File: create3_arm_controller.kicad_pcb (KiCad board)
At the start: 2 copper layers, 229.5 x 111 mm, 178 parts, among them IC1 TPS40192DRCT-TPS40192DRCT, J1 USB_C_Receptacle, J10 Conn_01x22_Female, J11 690-019-298-412, J12 Barrel_Jack, J13 Conn_01x02_Female, J14 Molex 470531000, J15 USB_OTG, J16 690-008-221-904, J17 Conn_01x03_Female, J18 Conn_01x03_Female, J19 Conn_01x03_Female, J2 USB_C_Receptacle, J20 Conn_01x03_Female, J21 Conn_01x03_Female, J22 Conn_01x03_Female, J23 Conn_01x03_Female, J24 Conn_01x03_Female, J25 Conn_01x03_Female, J26 Conn_01x03_Female, J27 Conn_01x03_Female, J28 Conn_01x03_Female, J4 Conn_02x07_Odd_Even, J5 Conn_01x03, J6 Conn_01x03, J7 THD-20-R, J8 Micro_SD_Card_Det, J9 Conn_01x22_Female, Q1 BUK9M17-30EX / BUK7M10-40E, Q2 BUK9M17-30EX / BUK7M10-40E, Q3 DMP3013SFV-7, U1 TUSB7340, U10 EMC2301-1-ACZL-TR, U11 74LVC1G07SE-7, U12 FSUSB42MUX, U13 USB2514B-I/M2, U14 TPD4EUSB30, U15 AP22653W6, U16 STM32F303VETx, U2 TPS2560, U3 TPS2560, U4 74LVC1G07SE-7, U5 74LVC1G07SE-7, U6 RT9742GGJ5, U7 RT9742SNGV, U8 AP64501SP-13, U9 PCF85063AT/AAZ, Y1 Crystal_Small, Y2 X32K768S301, Y3 24MHz

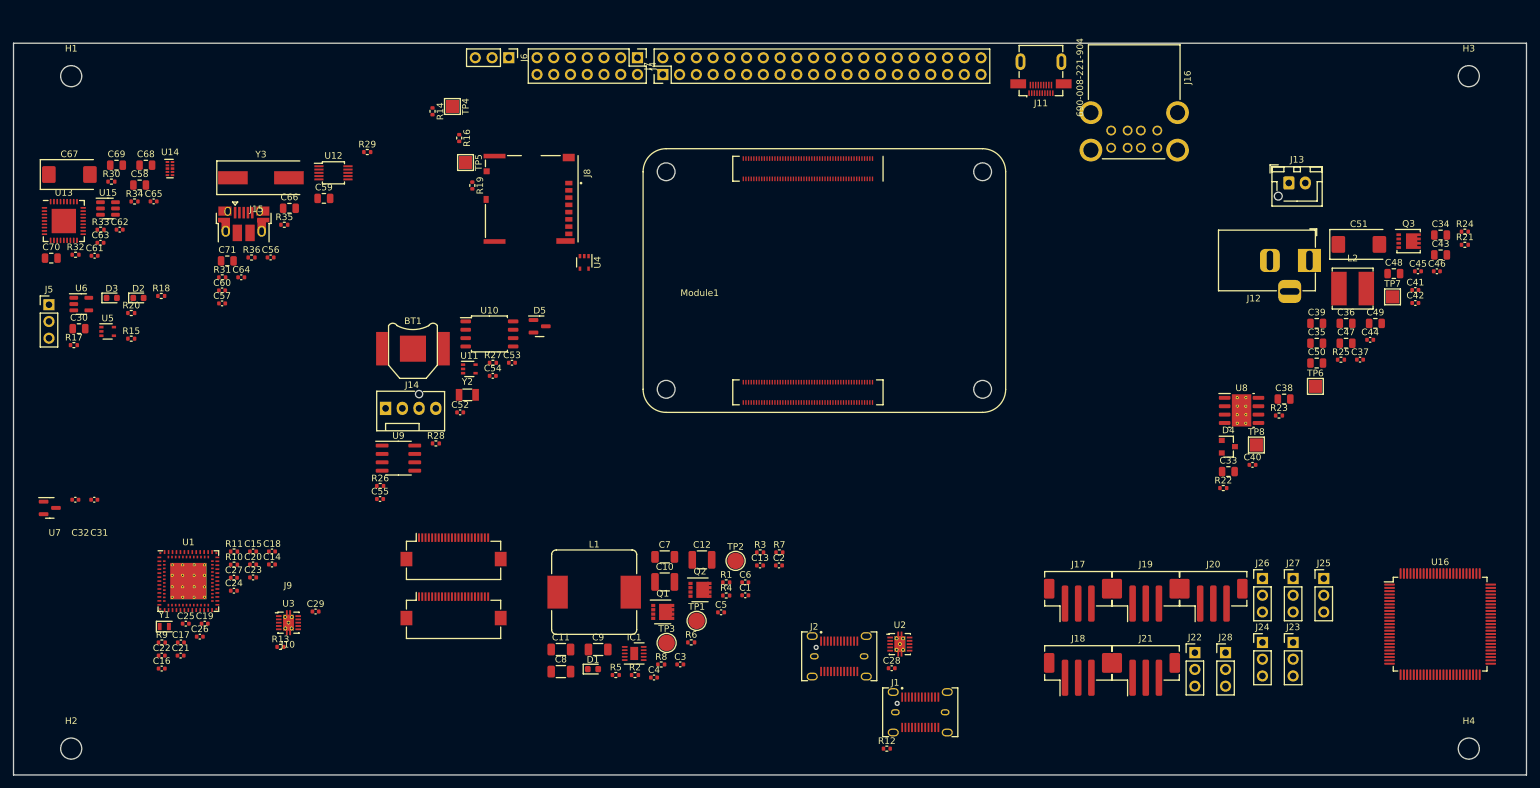
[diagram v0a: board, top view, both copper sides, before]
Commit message: Initial layout and all parts added. Some pins still not connected to power
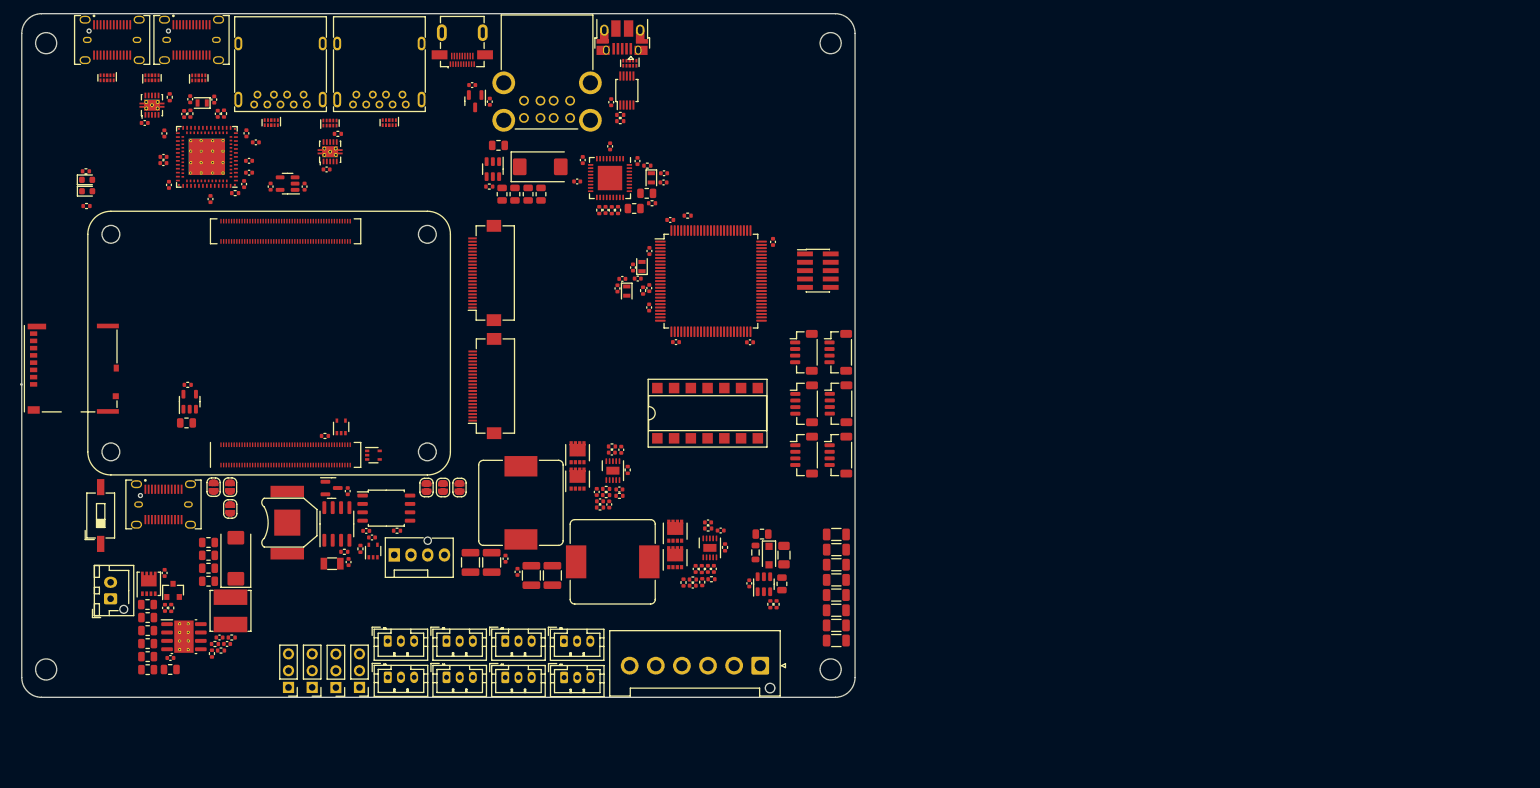
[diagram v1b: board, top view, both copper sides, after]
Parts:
- removed D1: LED, LED_SMD:LED_0603_1608Metric
- removed D2: LED Green, LED_SMD:LED_0603_1608Metric
- removed R16: nf, Resistor_SMD:R_0402_1005Metric
- removed R6: 100k, Resistor_SMD:R_0402_1005Metric
- removed R9: 4.7K, Resistor_SMD:R_0402_1005Metric
- removed TP1: Batt+, TestPoint:TestPoint_Pad_D2.5mm
- removed TP2: GND, TestPoint:TestPoint_Pad_D2.5mm
- removed TP3: 6V, TestPoint:TestPoint_Pad_D2.5mm
- removed TP4, TP5, TP6, TP7, TP8: TestPoint, TestPoint:TestPoint_Pad_2.0x2.0mm
- added C72: 10uF 35v, Capacitor_SMD:C_0805_2012Metric, F.Cu at (52.1, 126.0)
- added C73: 1.2nF, Capacitor_SMD:C_0402_1005Metric, F.Cu at (64.1, 122.1)
- added C74: 10uF, Capacitor_SMD:C_0805_2012Metric, F.Cu at (61.3, 106.7)
- added C75: 10uF, Capacitor_SMD:C_0805_2012Metric, F.Cu at (61.3, 110.6)
- added C76: 10uF, Capacitor_SMD:C_0805_2012Metric, F.Cu at (61.3, 112.6)
- added C77: 10uF, Capacitor_SMD:C_0805_2012Metric, F.Cu at (61.3, 108.7)
- added C78: 100uF, Capacitor_Tantalum_SMD:CP_EIA-7343-31_Kemet-D, F.Cu at (65.5, 109.1)
- added C79: 100nF, Capacitor_SMD:C_0402_1005Metric, F.Cu at (82.5, 99.0)
- added C80: 100nF, Capacitor_SMD:C_0402_1005Metric, F.Cu at (85.3, 105.0)
- added C81: 100nF, Capacitor_SMD:C_0402_1005Metric, F.Cu at (86.1, 106.0)
- added C82: 100nF, Capacitor_SMD:C_0402_1005Metric, F.Cu at (82.6, 109.7)
- added C83: 27pF, Capacitor_SMD:C_0402_1005Metric, F.Cu at (130.4, 50.7)
- added C84: 27pF, Capacitor_SMD:C_0402_1005Metric, F.Cu at (130.4, 52.1)
- added C85: 10uF, Capacitor_SMD:C_0805_2012Metric, F.Cu at (127.8, 53.8)
- added C86: 10uF, Capacitor_SMD:C_0805_2012Metric, F.Cu at (125.9, 56.1)
- added C87: 100nF, Capacitor_SMD:C_0402_1005Metric, F.Cu at (117.3, 52.0)
- added C88: 100nF, Capacitor_SMD:C_0402_1005Metric, F.Cu at (122.4, 40.0)
- added C89: 100nF, Capacitor_SMD:C_0402_1005Metric, F.Cu at (118.1, 48.7)
- added C90: 100nF, Capacitor_SMD:C_0402_1005Metric, F.Cu at (122.3, 46.6)
- added C91: 100nF, Capacitor_SMD:C_0402_1005Metric, F.Cu at (121.6, 56.3)
- added C92: 100nF, Capacitor_SMD:C_0402_1005Metric, F.Cu at (126.4, 48.9)
- added C93: 10uF, Capacitor_SMD:C_0805_2012Metric, F.Cu at (105.3, 46.5)
- added C94: 100uF, Capacitor_Tantalum_SMD:CP_EIA-7343-31_Kemet-D, F.Cu at (111.6, 49.8)
- added C95: 10uF, Capacitor_SMD:C_0805_2012Metric, F.Cu at (111.8, 53.9)
- added C96: 10uF, Capacitor_SMD:C_0805_2012Metric, F.Cu at (109.8, 53.9)
- added C97: 10uF, Capacitor_SMD:C_0805_2012Metric, F.Cu at (107.8, 53.9)
- added C98: 10uF, Capacitor_SMD:C_0805_2012Metric, F.Cu at (105.9, 53.9)
- added D6: MMBZ5242BLT3G, Diode_SMD:D_SOT-23_ANK, F.Cu at (56.0, 114.0)
- added D7: BAT54C-7-F, Package_TO_SOT_SMD:SOT-23, F.Cu at (80.0, 98.5)
- added F1: Fuse, Fuse:Fuse_1206_3216Metric, F.Cu at (148.6, 108.7)
- added IC2: TPS40192DRCT-TPS40192DRCT, Package_SON:VSON-10-1EP_3x3mm_P0.5mm_EP1.2x2mm, F.Cu at (137.4, 107.6)
- added IC3: LMR14010A, Package_TO_SOT_SMD:SOT-23-6, F.Cu at (145.6, 113.1)
- added J29: 690-019-298-412, Connector_HDMI:HDMI_Micro-D_Molex_46765-2x0x, F.Cu at (99.8, 29.4)
- added J3: Conn_01x03_Female, Connector_JST:JST_PH_B3B-PH-K_1x03_P2.00mm_Vertical, F.Cu at (106.3, 127.2)
- added J30: Conn_01x02_Female, Connector_JST:JST_XH_B2B-XH-AM_1x02_P2.50mm_Vertical, F.Cu at (46.5, 115.3)
- added J32: Molex 470531000, Connector:FanPinHeader_1x04_P2.54mm_Vertical, F.Cu at (89.5, 108.6)
- added J33: USB_OTG, CM4IO:USB_Micro-B_EDAC_UCON00686, F.Cu at (124.1, 29.0)
- added J34: 690-008-221-904, CM4IO:MOLEX_USB_67298-4090, F.Cu at (112.7, 37.0)
- added JP1: Jumper_2_Open, Jumper:SolderJumper-2_P1.3mm_Open_RoundedPad1.0x1.5mm, F.Cu at (94.4, 98.4)
- added JP2: Jumper_2_Open, Jumper:SolderJumper-2_P1.3mm_Open_RoundedPad1.0x1.5mm, F.Cu at (99.4, 98.4)
- added JP3: Jumper_2_Open, Jumper:SolderJumper-2_P1.3mm_Open_RoundedPad1.0x1.5mm, F.Cu at (64.6, 101.7)
- added JP4: Jumper_2_Open, Jumper:SolderJumper-2_P1.3mm_Open_RoundedPad1.0x1.5mm, F.Cu at (62.1, 98.3)
- added JP5: Jumper_2_Open, Jumper:SolderJumper-2_P1.3mm_Open_RoundedPad1.0x1.5mm, F.Cu at (64.6, 98.3)
- added JP6: Jumper_2_Open, Jumper:SolderJumper-2_P1.3mm_Open_RoundedPad1.0x1.5mm, F.Cu at (96.9, 98.4)
- added L3: 10uH, Inductor_SMD:L_0805_2012Metric, F.Cu at (144.3, 108.3)
- added L4: SRN6045TA-3R3Y, Inductor_SMD:L_Bourns_SRN6045TA, F.Cu at (64.7, 117.1)
- added Q4: BUK9M17-30EX / BUK7M10-40E, Package_SON:VSON-8_3.3x3.3mm_P0.65mm_NexFET, F.Cu at (132.1, 109.0)
- added Q5: DMP3013SFV-7, Package_SON:Diodes_PowerDI3333-8, F.Cu at (52.3, 113.0)
- added R37: 510K 1%, Resistor_SMD:R_0402_1005Metric, F.Cu at (84.4, 107.7)
- added R38: 2.2K 1%, Resistor_SMD:R_0402_1005Metric, F.Cu at (123.8, 42.8)
- added R39: 2.2K 1%, Resistor_SMD:R_0402_1005Metric, F.Cu at (123.8, 41.9)
- added R40: 36K 1%, Resistor_SMD:R_0402_1005Metric, F.Cu at (122.5, 56.3)
- added R41: 36K 1%, Resistor_SMD:R_0402_1005Metric, F.Cu at (120.6, 56.3)
- added R42: 36K 1%, Resistor_SMD:R_0402_1005Metric, F.Cu at (128.6, 55.3)
- added R43: 12K 1%, Resistor_SMD:R_0402_1005Metric, F.Cu at (127.9, 49.6)
- added R44: 36K 1%, Resistor_SMD:R_0402_1005Metric, F.Cu at (123.5, 56.3)
- added R45: 15K 1%, Resistor_SMD:R_0402_1005Metric, F.Cu at (103.9, 52.8)
- added SW1: SW_DIP_x01, Button_Switch_SMD:SW_DIP_SPSTx01_Slide_6.7x4.1mm_W8.61mm_P2.54mm_LowProfile, F.Cu at (45.0, 102.6)
- added U17: AP64501SP-13, Package_SO:SOIC-8-1EP_3.9x4.9mm_P1.27mm_EP2.95x4.9mm_Mask2.71x3.4mm_ThermalVias, F.Cu at (57.6, 121.0)
- added U18: PCF85063AT/AAZ, Package_SO:SOIC-8_3.9x4.9mm_P1.27mm, F.Cu at (80.8, 103.9)
- added U19: EMC2301-1-ACZL-TR, Package_SO:SOIC-8_5.23x5.23mm_P1.27mm, F.Cu at (88.3, 101.5)
- added U20: 74LVC1G07SE-7, Package_TO_SOT_SMD:SOT-353_SC-70-5, F.Cu at (86.3, 108.0)
- added U21: FSUSB42MUX, Package_SO:MSOP-10_3x3mm_P0.5mm, F.Cu at (124.8, 38.2)
- added U22: USB2514B-I/M2, Package_DFN_QFN:QFN-36-1EP_6x6mm_P0.5mm_EP3.7x3.7mm, F.Cu at (122.2, 51.5)
- added U23: TPD4EUSB30, Package_SON:USON-10_2.5x1.0mm_P0.5mm, F.Cu at (125.2, 34.0)
- added U24: AP22653W6, Package_TO_SOT_SMD:SOT-23-6, F.Cu at (104.5, 50.1)
- added Y4: X32K768S301, Crystal:Crystal_SMD_3215-2Pin_3.2x1.5mm, F.Cu at (80.1, 110.0)
- added Y5: 24MHz, Crystal:Crystal_SMD_2012-2Pin_2.0x1.2mm, F.Cu at (128.5, 51.4)
- C1: value 1000pF -> C
- C10: value 100uF -> 47uF; footprint Capacitor_SMD:C_1210_3225Metric -> Capacitor_SMD:C_1206_3216Metric
- C11: value 47uF -> 10uF
- C13: value 1uF -> 47uF; footprint Capacitor_SMD:C_0402_1005Metric -> Capacitor_SMD:C_1206_3216Metric
- C14: value 10pF -> 100uF; footprint Capacitor_SMD:C_0402_1005Metric -> Capacitor_SMD:C_1210_3225Metric
- C15: value 10pF -> 1uF
- C16: value C -> 1000pF
- C17: value C -> 100pF
- C18: value C -> 10nF
- C19, C28: value C -> 1uF
- C2: value 100pF -> C
- C20: value C -> 4.7uF
- C21: value C -> 470nF
- C22, C24: value C -> 10uF; footprint Capacitor_SMD:C_0402_1005Metric -> Capacitor_SMD:C_1206_3216Metric
- C23, C26: value C -> 47uF; footprint Capacitor_SMD:C_0402_1005Metric -> Capacitor_SMD:C_1206_3216Metric
- C25, C27: value C -> 100uF; footprint Capacitor_SMD:C_0402_1005Metric -> Capacitor_SMD:C_1210_3225Metric
- C3: value 10nF -> 1000pF
- C30, C47, C48, C49, C50: value 10u -> C; footprint Capacitor_SMD:C_0805_2012Metric -> Capacitor_SMD:C_0402_1005Metric
- C31, C32, C42, C52, C53, C54, C55: value 100n -> C
- C33, C34, C35, C36, C38, C39, C43: value 10u 35v -> C; footprint Capacitor_SMD:C_0805_2012Metric -> Capacitor_SMD:C_0402_1005Metric
- C37: value 100n 100v -> C
- C4: value 1uF -> 100pF
- C40, C41: value 100n -> 10pF
- C44, C46: value nf -> C
- C45: value 1.2nF -> C
- C5: value 4.7uF -> 10nF
- C51: value 100uF -> C; footprint Capacitor_Tantalum_SMD:CP_EIA-7343-31_Kemet-D -> Capacitor_SMD:C_0402_1005Metric
- C56: value 27pF -> 0.1uF
- C57: value 27pF -> 2.2uF; footprint Capacitor_SMD:C_0402_1005Metric -> Capacitor_SMD:C_0805_2012Metric
- C58, C59: value 10u -> 10uF
- C6: value 470nF -> 1uF
- C60, C61: value 100n -> 100nF
- C62, C63, C64, C65: value 100n -> 10uF 35v; footprint Capacitor_SMD:C_0402_1005Metric -> Capacitor_SMD:C_0805_2012Metric
- C66: value 10u -> 100nF 100v; footprint Capacitor_SMD:C_0805_2012Metric -> Capacitor_SMD:C_0402_1005Metric
- C67: value 100uF -> 10uF 35v; footprint Capacitor_Tantalum_SMD:CP_EIA-7343-31_Kemet-D -> Capacitor_SMD:C_0805_2012Metric
- C68: value 10u -> 10uF 35v
- C69, C70, C71: value 10u -> 100nF; footprint Capacitor_SMD:C_0805_2012Metric -> Capacitor_SMD:C_0402_1005Metric
- C7: value 10uF -> 4.7uF; footprint Capacitor_SMD:C_1206_3216Metric -> Capacitor_SMD:C_0402_1005Metric
- C8: value 47uF -> 470nF; footprint Capacitor_SMD:C_1206_3216Metric -> Capacitor_SMD:C_0402_1005Metric
- D3: value LED Red -> DIODE; footprint LED_SMD:LED_0603_1608Metric -> Diode_SMD:D_SOD-123F
- D4: value MMBZ5242BLT3G -> LED Green; footprint Diode_SMD:D_SOT-23_ANK -> LED_SMD:LED_0603_1608Metric
- D5: value BAT54C-7-F -> LED Red; footprint Package_TO_SOT_SMD:SOT-23 -> LED_SMD:LED_0603_1608Metric
- J10, J9: value Conn_01x22_Female -> Conn_01x03_Female; footprint Connector_FFC-FPC:Hirose_FH12-22S-0.5SH_1x22-1MP_P0.50mm_Horizontal -> Connector_JST:JST_PH_B3B-PH-K_1x03_P2.00mm_Vertical
- J11: value 690-019-298-412 -> Conn_01x03_Female; footprint Connector_HDMI:HDMI_Micro-D_Molex_46765-2x0x -> Connector_PinHeader_2.54mm:PinHeader_1x03_P2.54mm_Vertical
- J12: value Barrel_Jack -> Conn_01x03_Female; footprint Connector_BarrelJack:BarrelJack_Horizontal -> Connector_PinHeader_2.54mm:PinHeader_1x03_P2.54mm_Vertical
- J13: value Conn_01x02_Female -> Conn_01x03_Female; footprint Connector_JST:JST_XH_B2B-XH-AM_1x02_P2.50mm_Vertical -> Connector_PinHeader_2.54mm:PinHeader_1x03_P2.54mm_Vertical
- J14: value Molex 470531000 -> Conn_01x03_Female; footprint Connector:FanPinHeader_1x04_P2.54mm_Vertical -> Connector_PinHeader_2.54mm:PinHeader_1x03_P2.54mm_Vertical
- J15: value USB_OTG -> USB_C_Receptacle; footprint CM4IO:USB_Micro-B_EDAC_UCON00686 -> Connector_USB:USB_C_Receptacle_JAE_DX07S024WJ1R350
- J16: value 690-008-221-904 -> USB_C_Receptacle; footprint CM4IO:MOLEX_USB_67298-4090 -> Connector_USB:USB_C_Receptacle_JAE_DX07S024WJ1R350
- J17, J18: value Conn_01x03_Female -> USB3_A; footprint Connector_JST:JST_PH_B3B-PH-SM4-TB_1x03-1MP_P2.00mm_Vertical -> Connector_USB:USB3_A_Molex_48393-001
- J19: value Conn_01x03_Female -> Conn_01x06_Female; footprint Connector_JST:JST_PH_B3B-PH-SM4-TB_1x03-1MP_P2.00mm_Vertical -> Connector_JST:JST_VH_B6P-VH-FB-B_1x06_P3.96mm_Vertical
- J2: value USB_C_Receptacle -> Conn_ARM_JTAG_SWD_10; footprint Connector_USB:USB_C_Receptacle_JAE_DX07S024WJ1R350 -> Connector_PinHeader_1.27mm:PinHeader_2x05_P1.27mm_Vertical_SMD
- J20, J21: value Conn_01x03_Female -> Conn_01x04_Female; footprint Connector_JST:JST_PH_B3B-PH-SM4-TB_1x03-1MP_P2.00mm_Vertical -> Connector_JST:JST_SH_BM04B-SRSS-TB_1x04-1MP_P1.00mm_Vertical
- J22, J23, J24, J25: value Conn_01x03_Female -> Conn_01x04_Female; footprint Connector_PinHeader_2.54mm:PinHeader_1x03_P2.54mm_Vertical -> Connector_JST:JST_SH_BM04B-SRSS-TB_1x04-1MP_P1.00mm_Vertical
- J26: value Conn_01x03_Female -> Micro_SD_Card_Det; footprint Connector_PinHeader_2.54mm:PinHeader_1x03_P2.54mm_Vertical -> CM4IO:SDCARD_MOLEX_503398-1892
- J27, J28: value Conn_01x03_Female -> Conn_01x22_Female; footprint Connector_PinHeader_2.54mm:PinHeader_1x03_P2.54mm_Vertical -> Connector_FFC-FPC:Hirose_FH12-22S-0.5SH_1x22-1MP_P0.50mm_Horizontal
- J4: value Conn_02x07_Odd_Even -> Conn_01x03_Female; footprint Connector_PinHeader_2.54mm:PinHeader_2x07_P2.54mm_Vertical -> Connector_JST:JST_PH_B3B-PH-K_1x03_P2.00mm_Vertical
- J5, J6: value Conn_01x03 -> Conn_01x03_Female; footprint Connector_PinHeader_2.54mm:PinHeader_1x03_P2.54mm_Vertical -> Connector_JST:JST_PH_B3B-PH-K_1x03_P2.00mm_Vertical
- J7: value THD-20-R -> Conn_01x03_Female; footprint Connector_PinHeader_2.54mm:PinHeader_2x20_P2.54mm_Vertical -> Connector_JST:JST_PH_B3B-PH-K_1x03_P2.00mm_Vertical
- J8: value Micro_SD_Card_Det -> Conn_01x03_Female; footprint CM4IO:SDCARD_MOLEX_503398-1892 -> Connector_JST:JST_PH_B3B-PH-K_1x03_P2.00mm_Vertical
- L2: value SRN6045TA-3R3Y -> 1uH; footprint Inductor_SMD:L_Bourns_SRN6045TA -> Inductor_SMD:L_Bourns_SRP1245A
- Q3: value DMP3013SFV-7 -> BUK9M17-30EX / BUK7M10-40E; footprint Package_SON:Diodes_PowerDI3333-8 -> Package_SON:VSON-8_3.3x3.3mm_P0.65mm_NexFET
- R10: value 10K -> 20k
- R11: value 9.09K -> 2.61k
- R12: value 30.9K -> 4.22k
- R13: value 30.9K -> 12k
- R14: value 1k -> 100k
- R15: value 0R -> 100k
- R17: value 1k -> R
- R18: value nf -> R
- R19: value nf -> 4.7K
- R2: value 20k -> 2.18k
- R20: value 12K 1% -> 10K
- R21: value 12K 1% -> 9.09K
- R22: value 10R -> 30.9K
- R23: value 20K 1% -> 30.9K
- R24: value 12K 1% -> 33.2
- R25: value 2.2K 1% -> 10K
- R26: value 36K 1% -> 1k
- R27: value 510K 1% -> 0R
- R28: value 510K 1% -> 1k
- R29, R30: value 2.2K 1% -> 12K 1%
- R3: value 2.61k -> 20k
- R31: value 36K 1% -> 10R
- R32: value 36K 1% -> 20K 1%
- R33: value 36K 1% -> 12K 1%
- R34: value 12K 1% -> 2.2K 1%
- R36: value 15K 1% -> 510K 1%
- R4: value 4.22k -> 2.61k
- R5: value 12k -> 4.22k
- R8: value 1K -> 100k
- U1: value TUSB7340 -> TLV71211_SOT23-5; footprint Package_DFN_QFN:Texas_S-PWQFN-N100_EP5.5x5.5mm_ThermalVias -> Package_TO_SOT_SMD:SOT-23-5
- U10: value EMC2301-1-ACZL-TR -> TPD4EUSB30; footprint Package_SO:SOIC-8_5.23x5.23mm_P1.27mm -> Package_SON:USON-10_2.5x1.0mm_P0.5mm
- U11: value 74LVC1G07SE-7 -> TPS2560; footprint Package_TO_SOT_SMD:SOT-353_SC-70-5 -> Package_SON:VSON-10-1EP_3x3mm_P0.5mm_EP1.65x2.4mm_ThermalVias
- U12: value FSUSB42MUX -> TPS2560; footprint Package_SO:MSOP-10_3x3mm_P0.5mm -> Package_SON:VSON-10-1EP_3x3mm_P0.5mm_EP1.65x2.4mm_ThermalVias
- U13: value USB2514B-I/M2 -> 74LVC1G07SE-7; footprint Package_DFN_QFN:QFN-36-1EP_6x6mm_P0.5mm_EP3.7x3.7mm -> Package_TO_SOT_SMD:SOT-353_SC-70-5
- U14: value TPD4EUSB30 -> 74LVC1G07SE-7; footprint Package_SON:USON-10_2.5x1.0mm_P0.5mm -> Package_TO_SOT_SMD:SOT-353_SC-70-5
- U15: value AP22653W6 -> RT9742GGJ5; footprint Package_TO_SOT_SMD:SOT-23-6 -> Package_TO_SOT_SMD:SOT-23-5
- U16: value STM32F303VETx -> RT9742SNGV; footprint Package_QFP:LQFP-100_14x14mm_P0.5mm -> Package_TO_SOT_SMD:SOT-23
- U2: value TPS2560 -> 74LS125; footprint Package_SON:VSON-10-1EP_3x3mm_P0.5mm_EP1.65x2.4mm_ThermalVias -> Package_DIP:DIP-14_W7.62mm_SMDSocket_SmallPads
- U3: value TPS2560 -> STM32F303VETx; footprint Package_SON:VSON-10-1EP_3x3mm_P0.5mm_EP1.65x2.4mm_ThermalVias -> Package_QFP:LQFP-100_14x14mm_P0.5mm
- U4, U5: value 74LVC1G07SE-7 -> TPD4EUSB30; footprint Package_TO_SOT_SMD:SOT-353_SC-70-5 -> Package_SON:USON-10_2.5x1.0mm_P0.5mm
- U6: value RT9742GGJ5 -> TUSB7340; footprint Package_TO_SOT_SMD:SOT-23-5 -> Package_DFN_QFN:Texas_S-PWQFN-N100_EP5.5x5.5mm_ThermalVias
- U7: value RT9742SNGV -> TPD4EUSB30; footprint Package_TO_SOT_SMD:SOT-23 -> Package_SON:USON-10_2.5x1.0mm_P0.5mm
- U8: value AP64501SP-13 -> TPD4EUSB30; footprint Package_SO:SOIC-8-1EP_3.9x4.9mm_P1.27mm_EP2.95x4.9mm_Mask2.71x3.4mm_ThermalVias -> Package_SON:USON-10_2.5x1.0mm_P0.5mm
- U9: value PCF85063AT/AAZ -> TPD4EUSB30; footprint Package_SO:SOIC-8_3.9x4.9mm_P1.27mm -> Package_SON:USON-10_2.5x1.0mm_P0.5mm
- Y2: value X32K768S301 -> Crystal_Small; footprint Crystal:Crystal_SMD_3215-2Pin_3.2x1.5mm -> Crystal:Crystal_SMD_2012-2Pin_2.0x1.2mm
- Y3: value 24MHz -> Crystal_Small; footprint Crystal:Crystal_SMD_HC49-SD -> Crystal:Crystal_SMD_2012-2Pin_2.0x1.2mm
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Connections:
- C1 pad 1: +6V -> /CM4IOv5/+5v
- C1 pad 2: Net-(C1-Pad2) -> GND
- C10 pad 1: +6V -> /SUPPLIMENTAL_BATTERY
- C11 pad 1: +BATT -> /SUPPLIMENTAL_BATTERY
- C12 pad 1: +6V -> /REGULATED_MOTOR_6V
- C13 pad 1: +6V -> /SUPPLIMENTAL_BATTERY
- C14 pad 1: Net-(C14-Pad1) -> /REGULATED_MOTOR_6V
- C14 pad 2: Net-(C14-Pad2) -> GND
- C15 pad 1: Net-(C14-Pad1) -> /REGULATED_MOTOR_6V
- C15 pad 2: Net-(C15-Pad2) -> GND
- C16 pad 1: +1V1 -> /REGULATED_MOTOR_12V
- C16 pad 2: GND -> Net-(C16-Pad2)
- C17 pad 1: +1V1 -> Net-(C17-Pad1)
- C17 pad 2: GND -> /12vSwitchMode/FB_RESISTOR
- C18 pad 1: +1V1 -> Net-(C17-Pad1)
- C18 pad 2: GND -> Net-(C18-Pad2)
- C19 pad 1: +1V1 -> /SUPPLIMENTAL_BATTERY
- C2 pad 1: Net-(C2-Pad1) -> /CM4IOv5/+1.1v
- C2 pad 2: Net-(C2-Pad2) -> GND
- C20 pad 1: +1V1 -> Net-(C20-Pad1)
- C21 pad 1: +1V1 -> Net-(C21-Pad1)
- C21 pad 2: GND -> Net-(C21-Pad2)
- C22 pad 1: +3V3 -> /SUPPLIMENTAL_BATTERY
- C23 pad 1: +3V3 -> /SUPPLIMENTAL_BATTERY
- C24 pad 1: +3V3 -> /SUPPLIMENTAL_BATTERY
- C25 pad 1: +3V3 -> /REGULATED_MOTOR_12V
- C26 pad 1: +3V3 -> /SUPPLIMENTAL_BATTERY
- C27 pad 1: +3V3 -> /REGULATED_MOTOR_12V
- C28 pad 1: GND -> /REGULATED_MOTOR_12V
- C28 pad 2: +5V -> GND
- C29 pad 1: GND -> /CM4IOv5/GPIO2
- C29 pad 2: +5V -> GND
- C3 pad 1: Net-(C2-Pad1) -> /REGULATED_MOTOR_6V
- C30 pad 1: /CM4IOv5/CM4_GPIO ( Ethernet, GPIO, SDCARD)/SD_PWR -> Net-(C30-Pad1)
- C31 pad 1: /CM4IOv5/+5v -> Net-(C31-Pad1)
- C32 pad 1: /CM4IOv5/CM4_HighSpeed/HDMI_5v -> +3V3
- C33 pad 1: /CM4IOv5/+12v -> +3V3
- C34 pad 1: /CM4IOv5/+12v -> +3V3
- C35 pad 1: /CM4IOv5/+12v -> +3V3
- C36 pad 1: /CM4IOv5/+12v -> Net-(C36-Pad1)
- C38 pad 1: /CM4IOv5/+12v -> +3V3
- C39 pad 1: /CM4IOv5/+12v -> +3V3
- C4 pad 1: +BATT -> Net-(C4-Pad1)
- C4 pad 2: GND -> /12vSwitchMode1/FB_RESISTOR
- C41 pad 1: Net-(C41-Pad1) -> Net-(C40-Pad1)
- C41 pad 2: GND -> Net-(C41-Pad2)
- C42 pad 1: /CM4IOv5/+12v -> /CM4IOv5/+1.1v
- C42 pad 2: Net-(C42-Pad2) -> GND
- C43 pad 1: /CM4IOv5/+12v -> /CM4IOv5/+1.1v
- C44 pad 1: Net-(C44-Pad1) -> /CM4IOv5/+1.1v
- C45 pad 1: Net-(C45-Pad1) -> /CM4IOv5/+1.1v
- C46 pad 1: /CM4IOv5/+5v -> /CM4IOv5/+1.1v
- C46 pad 2: Net-(C46-Pad2) -> GND
- C47 pad 1: /CM4IOv5/+5v -> /CM4IOv5/+1.1v
- C48 pad 1: /CM4IOv5/+5v -> /CM4IOv5/+3.3v
- C49 pad 1: /CM4IOv5/+5v -> /CM4IOv5/+3.3v
- C5 pad 1: Net-(C5-Pad1) -> Net-(C4-Pad1)
- C5 pad 2: GND -> Net-(C5-Pad2)
- C50 pad 1: /CM4IOv5/+5v -> /CM4IOv5/+3.3v
- C51 pad 1: /CM4IOv5/+5v -> /CM4IOv5/+3.3v
- C52 pad 1: Net-(C52-Pad1) -> /CM4IOv5/+3.3v
- C54 pad 1: /CM4IOv5/+5v -> GND
- C54 pad 2: GND -> +5V
- C55 pad 1: Net-(C55-Pad1) -> GND
- C55 pad 2: /CM4IOv5/RTC , Wakeup, FAN/nRTC_INT -> +5V
- C56 pad 2: GND -> Net-(C56-Pad2)
- C57 pad 1: Net-(C57-Pad1) -> /SUPPLIMENTAL_BATTERY
- C58 pad 1: /CM4IOv5/+3.3v -> Net-(C58-Pad1)
- C59 pad 1: /CM4IOv5/+3.3v -> /CM4IOv5/CM4_GPIO ( Ethernet, GPIO, SDCARD)/SD_PWR
- C6 pad 1: Net-(C6-Pad1) -> /SUPPLIMENTAL_BATTERY
- C6 pad 2: Net-(C6-Pad2) -> GND
- C60 pad 1: /CM4IOv5/+3.3v -> /CM4IOv5/+5v
- C61 pad 1: /CM4IOv5/+3.3v -> /CM4IOv5/CM4_HighSpeed/HDMI_5v
- C62 pad 1: /CM4IOv5/+3.3v -> /CM4IOv5/+12v
- C63 pad 1: /CM4IOv5/+3.3v -> /CM4IOv5/+12v
- C64 pad 1: /CM4IOv5/+3.3v -> /CM4IOv5/+12v
- C65 pad 1: /CM4IOv5/+3.3v -> /CM4IOv5/+12v
- C66 pad 1: /CM4IOv5/+5v -> Net-(C66-Pad1)
- C67 pad 1: /CM4IOv5/USB2-HUB/VBUS -> /CM4IOv5/+12v
- C68 pad 1: /CM4IOv5/USB2-HUB/VBUS -> /CM4IOv5/+12v
- C69 pad 1: /CM4IOv5/USB2-HUB/VBUS -> Net-(C69-Pad1)
- C69 pad 2: GND -> Net-(C69-Pad2)
- C7 pad 1: +BATT -> Net-(C7-Pad1)
- C70 pad 1: /CM4IOv5/USB2-HUB/VBUS -> Net-(C70-Pad1)
- C71 pad 1: /CM4IOv5/USB2-HUB/VBUS -> /CM4IOv5/+12v
- C71 pad 2: GND -> Net-(C71-Pad2)
- C8 pad 1: +BATT -> Net-(C8-Pad1)
- C8 pad 2: GND -> Net-(C8-Pad2)
- C9 pad 1: +BATT -> /SUPPLIMENTAL_BATTERY
- D3 pad 1: Net-(D3-Pad1) -> Net-(C58-Pad1)
- D3 pad 2: /CM4IOv5/+3.3v -> Net-(D3-Pad2)
- D4 pad 1: /CM4IOv5/+12v -> Net-(D4-Pad1)
- D4 pad 2: Net-(C42-Pad2) -> /CM4IOv5/+3.3v
- D5 pad 1: Net-(BT1-Pad1) -> Net-(D5-Pad1)
- IC1 pad 2: Net-(C2-Pad2) -> /12vSwitchMode1/FB_RESISTOR
- IC1 pad 3: Net-(C2-Pad1) -> Net-(C4-Pad1)
- IC1 pad 4: +BATT -> /SUPPLIMENTAL_BATTERY
- IC1 pad 6: Net-(C5-Pad1) -> Net-(C7-Pad1)
- IC1 pad 8: Net-(C6-Pad2) -> Net-(C8-Pad2)
- IC1 pad 9: Net-(C6-Pad1) -> Net-(C8-Pad1)
- J1 pad A10: /CM4IOv5/USB3/P2_RX_N -> unconnected-(J1-PadA10)
- J1 pad A11: /CM4IOv5/USB3/P2_RX_P -> unconnected-(J1-PadA11)
- J1 pad A2: /CM4IOv5/USB3/P2_TX_P -> unconnected-(J1-PadA2)
- J1 pad A3: /CM4IOv5/USB3/P2_TX_N -> unconnected-(J1-PadA3)
- J1 pad A4: /CM4IOv5/USB3/USBC/P2_VBUS -> /CM4IOv5/+5V
- J1 pad A6: /CM4IOv5/USB3/P2_DP -> unconnected-(J1-PadA6)
- J1 pad A7: /CM4IOv5/USB3/P2_DN -> unconnected-(J1-PadA7)
- J1 pad A9: /CM4IOv5/USB3/USBC/P2_VBUS -> /CM4IOv5/+5V
- J1 pad B10: /CM4IOv5/USB3/P2_RX_N -> unconnected-(J1-PadB10)
- J1 pad B11: /CM4IOv5/USB3/P2_RX_P -> unconnected-(J1-PadB11)
- J1 pad B2: /CM4IOv5/USB3/P2_TX_P -> unconnected-(J1-PadB2)
- J1 pad B3: /CM4IOv5/USB3/P2_TX_N -> unconnected-(J1-PadB3)
- J1 pad B4: /CM4IOv5/USB3/USBC/P2_VBUS -> /CM4IOv5/+5V
- J1 pad B6: /CM4IOv5/USB3/P2_DP -> unconnected-(J1-PadB6)
- J1 pad B7: /CM4IOv5/USB3/P2_DN -> unconnected-(J1-PadB7)
- J1 pad B9: /CM4IOv5/USB3/USBC/P2_VBUS -> /CM4IOv5/+5V
- J10 pad 1: GND -> unconnected-(J10-Pad1)
- J10 pad 2: /CM4IOv5/CM4_HighSpeed/DSI1_D0_N -> unconnected-(J10-Pad2)
- J10 pad 3: /CM4IOv5/CM4_HighSpeed/DSI1_D0_P -> Net-(J10-Pad3)
- J11 pad 1: /CM4IOv5/CM4_HighSpeed/HDMI0_D2_P -> unconnected-(J11-Pad1)
- J11 pad 2: GND -> unconnected-(J11-Pad2)
- J11 pad 3: /CM4IOv5/CM4_HighSpeed/HDMI0_D2_N -> /MCU/TIM_3
- J12 pad 1: Net-(C37-Pad1) -> unconnected-(J12-Pad1)
- J12 pad 2: GND -> unconnected-(J12-Pad2)
- J12 pad 3: GND -> /MCU/TIM_1
- J13 pad 1: GND -> unconnected-(J13-Pad1)
- J13 pad 2: Net-(C37-Pad1) -> unconnected-(J13-Pad2)
- J14 pad 1: GND -> unconnected-(J14-Pad1)
- J14 pad 2: /CM4IOv5/+12v -> unconnected-(J14-Pad2)
- J14 pad 3: Net-(J14-Pad3) -> /MCU/TIM_4
- J17 pad 1: unconnected-(J17-Pad1) -> /CM4IOv5/USB3/USB3_CONN/P1_VBUS
- J17 pad 2: unconnected-(J17-Pad2) -> /CM4IOv5/USB3/P3_DN
- J17 pad 3: unconnected-(J17-Pad3) -> /CM4IOv5/USB3/P3_DP
- J18 pad 1: unconnected-(J18-Pad1) -> /CM4IOv5/USB3/USB3_CONN/P2_VBUS
- J18 pad 2: unconnected-(J18-Pad2) -> /CM4IOv5/USB3/P4_DN
- J18 pad 3: unconnected-(J18-Pad3) -> /CM4IOv5/USB3/P4_DP
- J19 pad 1: unconnected-(J19-Pad1) -> /SUPPLIMENTAL_BATTERY
- J19 pad 2: unconnected-(J19-Pad2) -> /SUPPLIMENTAL_BATTERY
- J19 pad 3: unconnected-(J19-Pad3) -> /SUPPLIMENTARY_BATTERY/COMMS_1
- J20 pad 1: unconnected-(J20-Pad1) -> GND
- J20 pad 2: unconnected-(J20-Pad2) -> +3V3
- J20 pad 3: unconnected-(J20-Pad3) -> /MCU/SCL2
- J21 pad 1: unconnected-(J21-Pad1) -> GND
- J21 pad 2: unconnected-(J21-Pad2) -> +3V3
- J21 pad 3: unconnected-(J21-Pad3) -> /MCU/SCL2
- J22 pad 1: unconnected-(J22-Pad1) -> GND
- J22 pad 2: unconnected-(J22-Pad2) -> +3V3
- J22 pad 3: unconnected-(J22-Pad3) -> /MCU/SCL3
- J23 pad 1: unconnected-(J23-Pad1) -> GND
- J23 pad 2: unconnected-(J23-Pad2) -> +3V3
- J23 pad 3: unconnected-(J23-Pad3) -> /MCU/SCL3
- J24 pad 1: unconnected-(J24-Pad1) -> GND
- J24 pad 2: unconnected-(J24-Pad2) -> +3V3
- J24 pad 3: unconnected-(J24-Pad3) -> /MCU/SCL1
- J25 pad 1: unconnected-(J25-Pad1) -> GND
- J25 pad 2: unconnected-(J25-Pad2) -> +3V3
- J25 pad 3: unconnected-(J25-Pad3) -> /MCU/SCL1
- J26 pad 1: unconnected-(J26-Pad1) -> /CM4IOv5/CM4_GPIO ( Ethernet, GPIO, SDCARD)/SD_DAT2
- J26 pad 2: unconnected-(J26-Pad2) -> /CM4IOv5/CM4_GPIO ( Ethernet, GPIO, SDCARD)/SD_DAT3
- J26 pad 3: unconnected-(J26-Pad3) -> /CM4IOv5/CM4_GPIO ( Ethernet, GPIO, SDCARD)/SD_CMD
- J27 pad 1: unconnected-(J27-Pad1) -> GND
- J27 pad 2: unconnected-(J27-Pad2) -> /CM4IOv5/CM4_HighSpeed/CAM1_D0_N
- J27 pad 3: unconnected-(J27-Pad3) -> /CM4IOv5/CM4_HighSpeed/CAM1_D0_P
- J28 pad 1: unconnected-(J28-Pad1) -> GND
- J28 pad 2: unconnected-(J28-Pad2) -> /CM4IOv5/CM4_HighSpeed/DSI1_D0_N
- J28 pad 3: unconnected-(J28-Pad3) -> /CM4IOv5/CM4_HighSpeed/DSI1_D0_P
- J4 pad 1: GND -> unconnected-(J4-Pad1)
- J4 pad 2: /CM4IOv5/CM4_GPIO ( Ethernet, GPIO, SDCARD)/nRPIBOOT -> unconnected-(J4-Pad2)
- J4 pad 3: GND -> /MCU/USART_1_RX
- J5 pad 1: /CM4IOv5/CM4_GPIO ( Ethernet, GPIO, SDCARD)/WL_nDis -> unconnected-(J5-Pad1)
- J5 pad 2: GND -> unconnected-(J5-Pad2)
- J5 pad 3: /CM4IOv5/CM4_GPIO ( Ethernet, GPIO, SDCARD)/BT_nDis -> /MCU/USART_2_RX
- J6 pad 1: /CM4IOv5/CM4_GPIO ( Ethernet, GPIO, SDCARD)/GLOBAL_EN -> unconnected-(J6-Pad1)
- J6 pad 2: GND -> unconnected-(J6-Pad2)
- J6 pad 3: /CM4IOv5/CM4_GPIO ( Ethernet, GPIO, SDCARD)/RUN_PG -> /MCU/USART_2_RX
- J7 pad 1: /CM4IOv5/+3.3v -> unconnected-(J7-Pad1)
- J7 pad 2: /CM4IOv5/+5v -> unconnected-(J7-Pad2)
- J7 pad 3: /CM4IOv5/CM4_GPIO ( Ethernet, GPIO, SDCARD)/GPIO2 -> /MCU/USART_3_RX
- J8 pad 1: /CM4IOv5/CM4_GPIO ( Ethernet, GPIO, SDCARD)/SD_DAT2 -> unconnected-(J8-Pad1)
- J8 pad 2: /CM4IOv5/CM4_GPIO ( Ethernet, GPIO, SDCARD)/SD_DAT3 -> unconnected-(J8-Pad2)
- J8 pad 3: /CM4IOv5/CM4_GPIO ( Ethernet, GPIO, SDCARD)/SD_CMD -> /MCU/USART_3_RX
- J9 pad 1: GND -> unconnected-(J9-Pad1)
- J9 pad 2: /CM4IOv5/CM4_HighSpeed/CAM1_D0_N -> unconnected-(J9-Pad2)
- J9 pad 3: /CM4IOv5/CM4_HighSpeed/CAM1_D0_P -> Net-(J10-Pad3)
- L1 pad 1: Net-(C6-Pad1) -> Net-(C8-Pad1)
- L1 pad 2: +6V -> /REGULATED_MOTOR_6V
- L2 pad 1: Net-(L2-Pad1) -> Net-(C21-Pad1)
- L2 pad 2: /CM4IOv5/+5v -> /REGULATED_MOTOR_12V
- Module1 pad 34: /CM4IOv5/CM4_GPIO ( Ethernet, GPIO, SDCARD)/GPIO5 -> /CM4IOv5/GPIO5
- Module1 pad 54: /CM4IOv5/CM4_GPIO ( Ethernet, GPIO, SDCARD)/GPIO4 -> /CM4IOv5/GPIO4
- Module1 pad 56: /CM4IOv5/CM4_GPIO ( Ethernet, GPIO, SDCARD)/GPIO3 -> /CM4IOv5/GPIO3
- Module1 pad 58: /CM4IOv5/CM4_GPIO ( Ethernet, GPIO, SDCARD)/GPIO2 -> /CM4IOv5/GPIO2
- Q1 pad 1: Net-(C6-Pad1) -> Net-(C8-Pad1)
- Q1 pad 2: Net-(C6-Pad1) -> Net-(C8-Pad1)
- Q1 pad 3: Net-(C6-Pad1) -> Net-(C8-Pad1)
- Q1 pad 5: +BATT -> /SUPPLIMENTAL_BATTERY
- Q2 pad 5: Net-(C6-Pad1) -> Net-(C8-Pad1)
- Q3 pad 1: /CM4IOv5/+12v -> Net-(C21-Pad1)
- Q3 pad 2: /CM4IOv5/+12v -> Net-(C21-Pad1)
- Q3 pad 3: /CM4IOv5/+12v -> Net-(C21-Pad1)
- Q3 pad 4: Net-(C42-Pad2) -> Net-(IC2-Pad10)
- Q3 pad 5: Net-(C37-Pad1) -> /SUPPLIMENTAL_BATTERY
- R1 pad 1: Net-(C2-Pad2) -> GND
- R1 pad 2: GND -> /12vSwitchMode/FB_RESISTOR
- R10 pad 1: +3V3 -> /REGULATED_MOTOR_12V
- R10 pad 2: Net-(R10-Pad2) -> /12vSwitchMode/FB_RESISTOR
- R11 pad 1: Net-(R11-Pad1) -> /12vSwitchMode/FB_RESISTOR
- R11 pad 2: Net-(R11-Pad2) -> Net-(C16-Pad2)
- R12 pad 1: Net-(R12-Pad1) -> Net-(C18-Pad2)
- R12 pad 2: GND -> /12vSwitchMode/FB_RESISTOR
- R13 pad 1: Net-(R13-Pad1) -> Net-(C17-Pad1)
- R14 pad 1: Net-(D2-Pad1) -> Net-(C20-Pad1)
- R14 pad 2: Net-(Module1-Pad21) -> Net-(IC2-Pad5)
- R15 pad 1: /CM4IOv5/+3.3v -> Net-(C21-Pad1)
- R15 pad 2: /CM4IOv5/CM4_GPIO ( Ethernet, GPIO, SDCARD)/GPIO_VREF -> Net-(C21-Pad2)
- R17 pad 1: Net-(D3-Pad1) -> +3V3
- R17 pad 2: Net-(R17-Pad2) -> /CM4IOv5/GPIO2
- R18 pad 1: /CM4IOv5/+3.3v -> /CM4IOv5/GPIO3
- R18 pad 2: Net-(J8-Pad10) -> GND
- R19 pad 1: /CM4IOv5/CM4_GPIO ( Ethernet, GPIO, SDCARD)/Reserved -> GND
- R19 pad 2: Net-(J8-Pad9) -> Net-(R19-Pad2)
- R2 pad 1: +6V -> GND
- R2 pad 2: Net-(C2-Pad2) -> /12vSwitchMode1/FB_RESISTOR
- R20 pad 1: /CM4IOv5/+3.3v -> +3V3
- R20 pad 2: /CM4IOv5/CM4_GPIO ( Ethernet, GPIO, SDCARD)/SD_PWR_ON -> Net-(R20-Pad2)
- R21 pad 1: Net-(C42-Pad2) -> Net-(R21-Pad1)
- R21 pad 2: GND -> Net-(R21-Pad2)
- R22 pad 1: Net-(L2-Pad1) -> Net-(R22-Pad1)
- R22 pad 2: Net-(C40-Pad1) -> GND
- R23 pad 1: Net-(C44-Pad1) -> Net-(R23-Pad1)
- R23 pad 2: Net-(C45-Pad1) -> GND
- R24 pad 1: /CM4IOv5/+5v -> +3V3
- R24 pad 2: Net-(C46-Pad2) -> Net-(IC3-Pad3)
- R25 pad 1: Net-(C46-Pad2) -> GND
- R25 pad 2: GND -> Net-(IC3-Pad3)
- R26 pad 1: Net-(J14-Pad3) -> Net-(D4-Pad1)
- R26 pad 2: /CM4IOv5/+3.3v -> Net-(Module1-Pad21)
- R27 pad 1: /CM4IOv5/RTC , Wakeup, FAN/nRTC_INT -> /CM4IOv5/+3.3v
- R27 pad 2: /CM4IOv5/+5v -> /CM4IOv5/CM4_GPIO ( Ethernet, GPIO, SDCARD)/GPIO_VREF
- R28 pad 1: Net-(C55-Pad1) -> Net-(D5-Pad1)
- R28 pad 2: /CM4IOv5/+5v -> Net-(R28-Pad2)
- R29 pad 1: /CM4IOv5/CM4_HighSpeed/USBOTG_ID -> /CM4IOv5/+3.3v
- R29 pad 2: GND -> /CM4IOv5/CM4_GPIO ( Ethernet, GPIO, SDCARD)/SD_PWR_ON
- R3 pad 1: Net-(C2-Pad2) -> /REGULATED_MOTOR_6V
- R3 pad 2: Net-(C1-Pad2) -> /12vSwitchMode1/FB_RESISTOR
- R30 pad 1: Net-(J15-Pad1) -> Net-(C71-Pad2)
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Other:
- board size 229.5 x 111 mm -> 126.4 x 103.7 mm

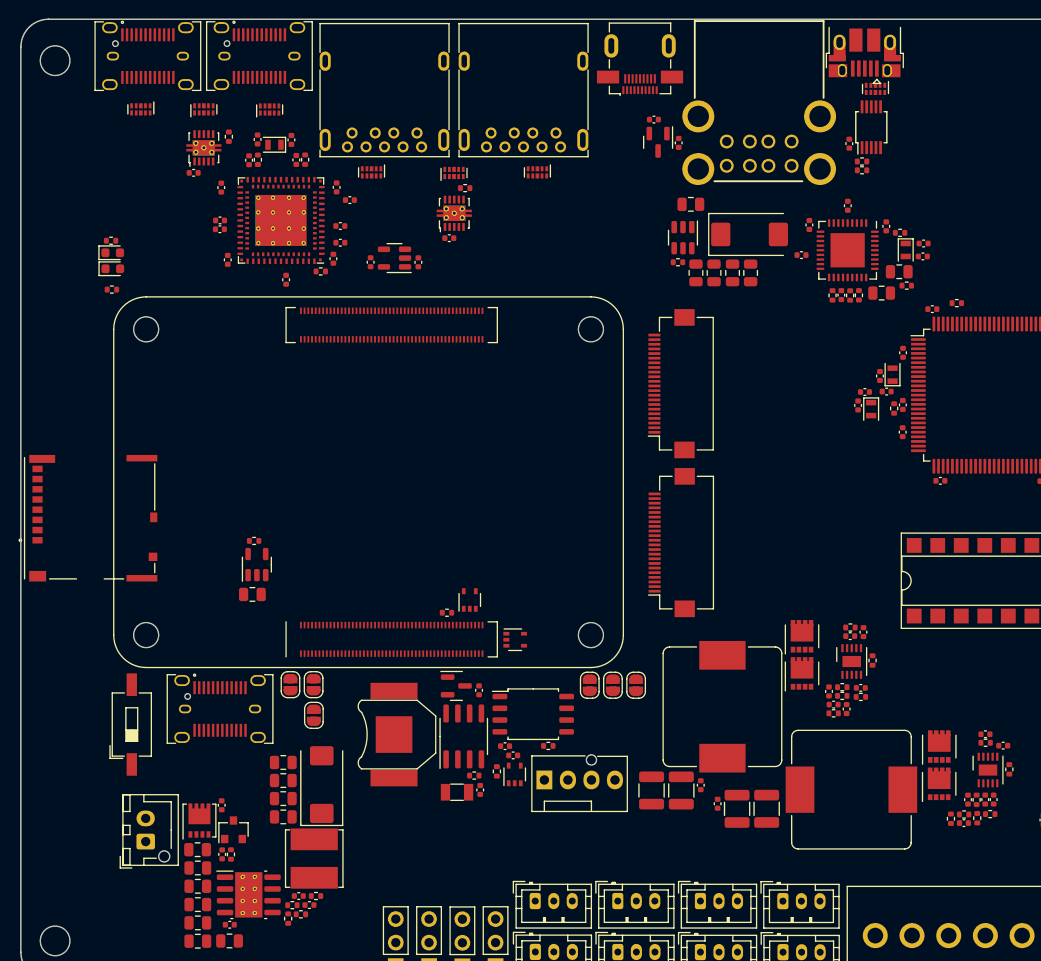
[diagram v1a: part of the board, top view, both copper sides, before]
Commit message: Diff pairs routed
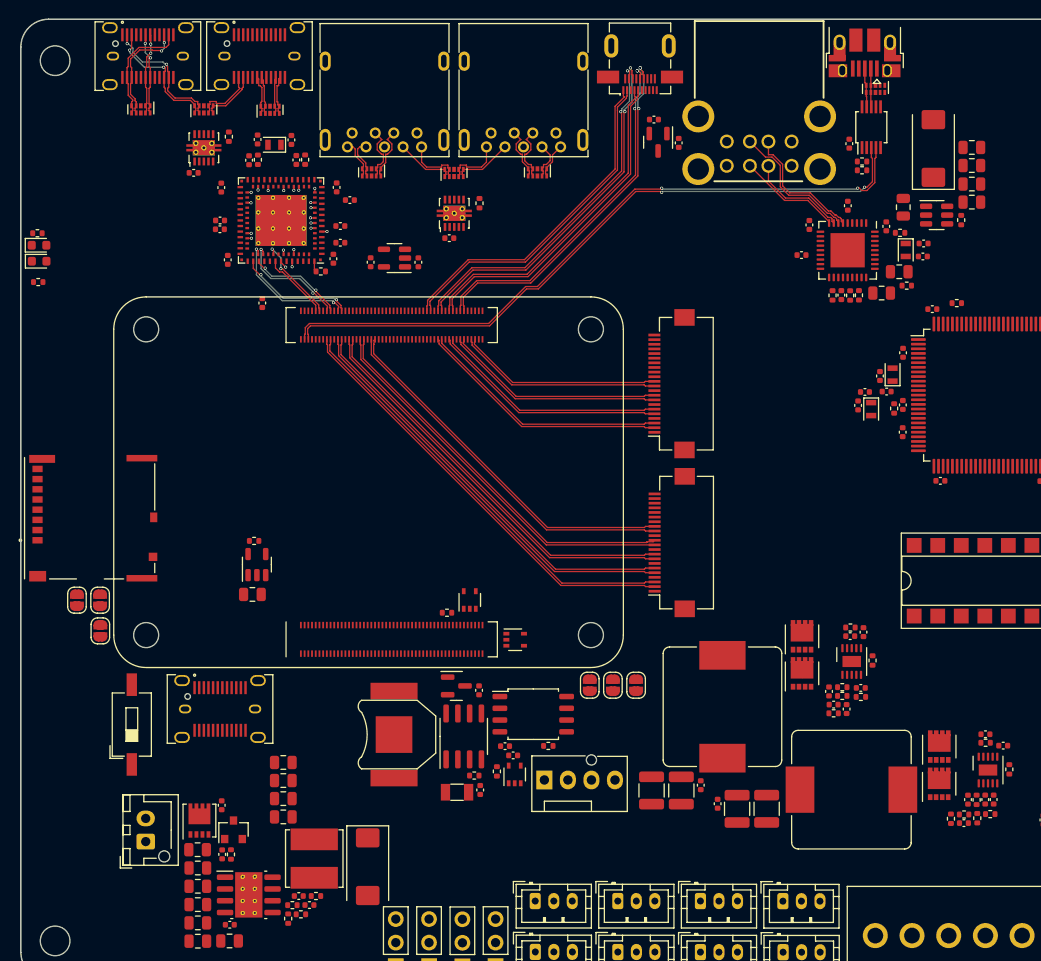
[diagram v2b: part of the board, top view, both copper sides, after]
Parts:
- moved R45 30.9 mm to (134.5, 48.2), turned to -90 degrees
- moved C98 30.7 mm to (135.6, 46.3), turned to 0 degrees
- moved C97 29.4 mm to (135.6, 44.3), turned to 0 degrees
- moved C96 28.3 mm to (135.6, 42.3), turned to 0 degrees
- moved U24 27.5 mm to (131.8, 47.7), turned to 0 degrees
- moved C95 27.4 mm to (135.6, 40.4), turned to 0 degrees
- moved JP3 24.8 mm to (41.6, 92.5)
- moved JP4 24.8 mm to (39.1, 89.2)
- moved JP5 24.8 mm to (41.6, 89.2)
- moved C93 22.9 mm to (128.2, 46.8), turned to -90 degrees
- moved C94 21.9 mm to (131.5, 40.5), turned to 90 degrees
- moved C78 10.2 mm to (70.4, 118.0), turned to -90 degrees
- moved D5 7.99 mm to (35.0, 50.9)
- moved R26 7.99 mm to (34.9, 54.9)
- moved D4 7.99 mm to (35.0, 52.6)
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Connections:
- U10 pad 1: /CM4IOv5/USB3/P4_DP -> /CM4IOv5/USB3/P4_DN
- U10 pad 10: /CM4IOv5/USB3/P4_DP -> /CM4IOv5/USB3/P4_DN
- U10 pad 2: /CM4IOv5/USB3/P4_DN -> /CM4IOv5/USB3/P4_DP
- U10 pad 9: /CM4IOv5/USB3/P4_DN -> /CM4IOv5/USB3/P4_DP
- U22 pad 1: /CM4IOv5/USB2-HUB/HD1_N -> /CM4IOv5/USB_1_N
- U22 pad 2: /CM4IOv5/USB2-HUB/HD1_P -> /CM4IOv5/USB_1_P
- U22 pad 3: /CM4IOv5/USB2-HUB/HD2_N -> /CM4IOv5/USB_2_N
- U22 pad 4: /CM4IOv5/USB2-HUB/HD2_P -> /CM4IOv5/USB_2_P
- U22 pad 6: /CM4IOv5/USB_1_N -> /CM4IOv5/USB2-HUB/HD2_N
- U22 pad 7: /CM4IOv5/USB_1_P -> /CM4IOv5/USB2-HUB/HD2_P
- U22 pad 8: /CM4IOv5/USB_2_N -> /CM4IOv5/USB2-HUB/HD1_N
- U22 pad 9: /CM4IOv5/USB_2_P -> /CM4IOv5/USB2-HUB/HD1_P
- U4 pad 4: /CM4IOv5/USB3/P1_RX_P -> /CM4IOv5/USB3/P1_RX_N
- U4 pad 5: /CM4IOv5/USB3/P1_RX_N -> /CM4IOv5/USB3/P1_RX_P
- U4 pad 6: /CM4IOv5/USB3/P1_RX_N -> /CM4IOv5/USB3/P1_RX_P
- U4 pad 7: /CM4IOv5/USB3/P1_RX_P -> /CM4IOv5/USB3/P1_RX_N
- U5 pad 1: /CM4IOv5/USB3/P1_TX_P -> /CM4IOv5/USB3/P1_TX_N
- U5 pad 10: /CM4IOv5/USB3/P1_TX_P -> /CM4IOv5/USB3/P1_TX_N
- U5 pad 2: /CM4IOv5/USB3/P1_TX_N -> /CM4IOv5/USB3/P1_TX_P
- U5 pad 9: /CM4IOv5/USB3/P1_TX_N -> /CM4IOv5/USB3/P1_TX_P
- U7 pad 1: /CM4IOv5/USB3/P2_DP -> /CM4IOv5/USB3/P2_DN
- U7 pad 10: /CM4IOv5/USB3/P2_DP -> /CM4IOv5/USB3/P2_DN
- U7 pad 2: /CM4IOv5/USB3/P2_DN -> /CM4IOv5/USB3/P2_DP
- U7 pad 4: /CM4IOv5/USB3/P2_TX_P -> /CM4IOv5/USB3/P2_TX_N
- U7 pad 5: /CM4IOv5/USB3/P2_TX_N -> /CM4IOv5/USB3/P2_TX_P
- U7 pad 6: /CM4IOv5/USB3/P2_TX_N -> /CM4IOv5/USB3/P2_TX_P
- U7 pad 7: /CM4IOv5/USB3/P2_TX_P -> /CM4IOv5/USB3/P2_TX_N
- U7 pad 9: /CM4IOv5/USB3/P2_DN -> /CM4IOv5/USB3/P2_DP
- U8 pad 1: /CM4IOv5/USB3/P4_TX_P -> /CM4IOv5/USB3/P4_TX_N
- U8 pad 10: /CM4IOv5/USB3/P4_TX_P -> /CM4IOv5/USB3/P4_TX_N
- U8 pad 2: /CM4IOv5/USB3/P4_TX_N -> /CM4IOv5/USB3/P4_TX_P
- U8 pad 4: /CM4IOv5/USB3/P3_RX_P -> /CM4IOv5/USB3/P3_RX_N
- U8 pad 5: /CM4IOv5/USB3/P3_RX_N -> /CM4IOv5/USB3/P3_RX_P
- U8 pad 6: /CM4IOv5/USB3/P3_RX_N -> /CM4IOv5/USB3/P3_RX_P
- U8 pad 7: /CM4IOv5/USB3/P3_RX_P -> /CM4IOv5/USB3/P3_RX_N
- U8 pad 9: /CM4IOv5/USB3/P4_TX_N -> /CM4IOv5/USB3/P4_TX_P
- U9 pad 4: /CM4IOv5/USB3/P3_DP -> /CM4IOv5/USB3/P3_DN
- U9 pad 5: /CM4IOv5/USB3/P3_DN -> /CM4IOv5/USB3/P3_DP
- U9 pad 6: /CM4IOv5/USB3/P3_DN -> /CM4IOv5/USB3/P3_DP
- U9 pad 7: /CM4IOv5/USB3/P3_DP -> /CM4IOv5/USB3/P3_DN
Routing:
- net /CM4IOv5/CM4_HighSpeed/USB2_N: track 0.00 -> 73.4 mm, vias 0 -> 2
- net /CM4IOv5/CM4_HighSpeed/USB2_P: track 0.00 -> 72.5 mm, vias 0 -> 2
- net /CM4IOv5/CM4_HighSpeed/CAM1_D0_N: track 0.00 -> 47.2 mm
- net /CM4IOv5/CM4_HighSpeed/CAM1_D0_P: track 0.00 -> 46.8 mm
- net /CM4IOv5/CM4_HighSpeed/CAM1_D1_N: track 0.00 -> 45.6 mm
- net /CM4IOv5/CM4_HighSpeed/CAM1_D1_P: track 0.00 -> 45.2 mm
- net /CM4IOv5/CM4_HighSpeed/CAM1_C_N: track 0.00 -> 43.9 mm
- net /CM4IOv5/CM4_HighSpeed/CAM1_C_P: track 0.00 -> 43.5 mm
- net /CM4IOv5/CM4_HighSpeed/CAM1_D2_N: track 0.00 -> 42.2 mm
- net /CM4IOv5/CM4_HighSpeed/CAM1_D2_P: track 0.00 -> 41.9 mm
- net /CM4IOv5/CM4_HighSpeed/CAM1_D3_N: track 0.00 -> 40.1 mm
- net /CM4IOv5/CM4_HighSpeed/CAM1_D3_P: track 0.00 -> 39.8 mm
- net /CM4IOv5/CM4_HighSpeed/HDMI0_D1_N: track 0.00 -> 39.6 mm, vias 0 -> 2
- net /CM4IOv5/CM4_HighSpeed/HDMI0_CK_N: track 0.00 -> 39.3 mm, vias 0 -> 3
- net /CM4IOv5/CM4_HighSpeed/HDMI0_D1_P: track 0.00 -> 39.1 mm, vias 0 -> 2
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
